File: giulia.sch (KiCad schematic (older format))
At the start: 129 parts, among them J1 AVR-ISP-6, J2 0548190519, SW1 RESET, SW2 BOOT, U1 ATmega32A-PU, Y1 16 MHz

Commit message: moved USB footprint to own lib
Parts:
- removed J2: 0548190519, digikey-footprints:USB_Mini_B_Female_548190519, symbol dk_USB-DVI-HDMI-Connectors:0548190519
- added J2: 0548190519, giulia:USB_Mini_B_Female_548190519, symbol giulia:0548190519
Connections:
- net GND: now also J2.1
- net VCC: now also J2.5
- net at D48.1 (K), R2.2: now also J2.3
- net at D49.1 (K), R3.2: now also J2.4
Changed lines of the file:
@@
 	5200 5850 5050 5850
-$Comp
-L dk_USB-DVI-HDMI-Connectors:0548190519 J2
-U 1 1 61732FEC
-P 4650 6950
-F 0 "J2" H 4675 7602 60  0000 C CNN
-F 1 "0548190519" H 4675 7496 60  0000 C CNN
-F 2 "digikey-footprints:USB_Mini_B_Female_548190519" H 4850 7150 60  0001 L CNN
-F 3 "https://www.molex.com/pdm_docs/sd/548190519_sd.pdf" H 4850 7250 60  0001 L CNN
-F 4 "WM17115-ND" H 4850 7350 60  0001 L CNN "Digi-Key_PN"
-F 5 "0548190519" H 4850 7450 60  0001 L CNN "MPN"
-F 6 "Connectors, Interconnects" H 4850 7550 60  0001 L CNN "Category"
-F 7 "USB, DVI, HDMI Connectors" H 4850 7650 60  0001 L CNN "Family"
-F 8 "https://www.molex.com/pdm_docs/sd/548190519_sd.pdf" H 4850 7750 60  0001 L CNN "DK_Datasheet_Link"
-F 9 "/product-detail/en/molex/0548190519/WM17115-ND/773802" H 4850 7850 60  0001 L CNN "DK_Detail_Page"
-F 10 "CONN RCPT USB2.0 MINI B 5P R/A" H 4850 7950 60  0001 L CNN "Description"
-F 11 "Molex" H 4850 8050 60  0001 L CNN "Manufacturer"
-F 12 "Active" H 4850 8150 60  0001 L CNN "Status"
-	1    4650 6950
-	1    0    0    -1
-$EndComp
 $Comp
 L power:VCC #PWR011
@@
 $EndComp
 Wire Wire Line
-	4950 7150 6300 7150
-Wire Wire Line
 	6300 7100 6300 7150
 Connection ~ 6300 7150
 Wire Wire Line
 	6300 7150 6450 7150
-Wire Wire Line
-	6750 6750 5850 6750
 Connection ~ 5850 7050
 Wire Wire Line
@@
 	1    0    0    -1
 $EndComp
+$Comp
+L giulia:0548190519 J2
+U 1 1 616D264C
+P 4650 6950
+F 0 "J2" H 4675 7602 60  0000 C CNN
+F 1 "0548190519" H 4675 7496 60  0000 C CNN
+F 2 "giulia:USB_Mini_B_Female_548190519" H 4850 7150 60  0001 L CNN
+F 3 "https://www.molex.com/pdm_docs/sd/548190519_sd.pdf" H 4850 7250 60  0001 L CNN
+F 4 "WM17115-ND" H 4850 7350 60  0001 L CNN "Digi-Key_PN"
+F 5 "0548190519" H 4850 7450 60  0001 L CNN "MPN"
+F 6 "Connectors, Interconnects" H 4850 7550 60  0001 L CNN "Category"
+F 7 "USB, DVI, HDMI Connectors" H 4850 7650 60  0001 L CNN "Family"
+F 8 "https://www.molex.com/pdm_docs/sd/548190519_sd.pdf" H 4850 7750 60  0001 L CNN "DK_Datasheet_Link"
+F 9 "/product-detail/en/molex/0548190519/WM17115-ND/773802" H 4850 7850 60  0001 L CNN "DK_Detail_Page"
+F 10 "CONN RCPT USB2.0 MINI B 5P R/A" H 4850 7950 60  0001 L CNN "Description"
+F 11 "Molex" H 4850 8050 60  0001 L CNN "Manufacturer"
+F 12 "Active" H 4850 8150 60  0001 L CNN "Status"
+	1    4650 6950
+	1    0    0    -1
+$EndComp
+Wire Wire Line
+	4950 7150 6300 7150
+Wire Wire Line
+	5850 6750 6750 6750
 $EndSCHEMATC

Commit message: some PCB finishing touches
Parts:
- D48, D49: footprint Diode_THT:D_DO-35_SOD27_P7.62mm_Horizontal -> giulia:D_DO-35_SOD27_P7.62mm_Zener
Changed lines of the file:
@@
 F 0 "D49" V 5950 6700 50  0000 L CNN
 F 1 "3,6 V" V 5850 6650 50  0000 L CNN
-F 2 "Diode_THT:D_DO-35_SOD27_P7.62mm_Horizontal" V 5850 6950 50  0001 C CNN
+F 2 "giulia:D_DO-35_SOD27_P7.62mm_Zener" V 5850 6950 50  0001 C CNN
 F 3 "~" V 5850 6950 50  0001 C CNN
 	1    5850 6950
@@
 F 0 "D48" V 5400 7050 50  0000 R CNN
 F 1 "3,6 V" V 5300 7100 50  0000 R CNN
-F 2 "Diode_THT:D_DO-35_SOD27_P7.62mm_Horizontal" V 5350 6850 50  0001 C CNN
+F 2 "giulia:D_DO-35_SOD27_P7.62mm_Zener" V 5350 6850 50  0001 C CNN
 F 3 "~" V 5350 6850 50  0001 C CNN
 	1    5350 6850

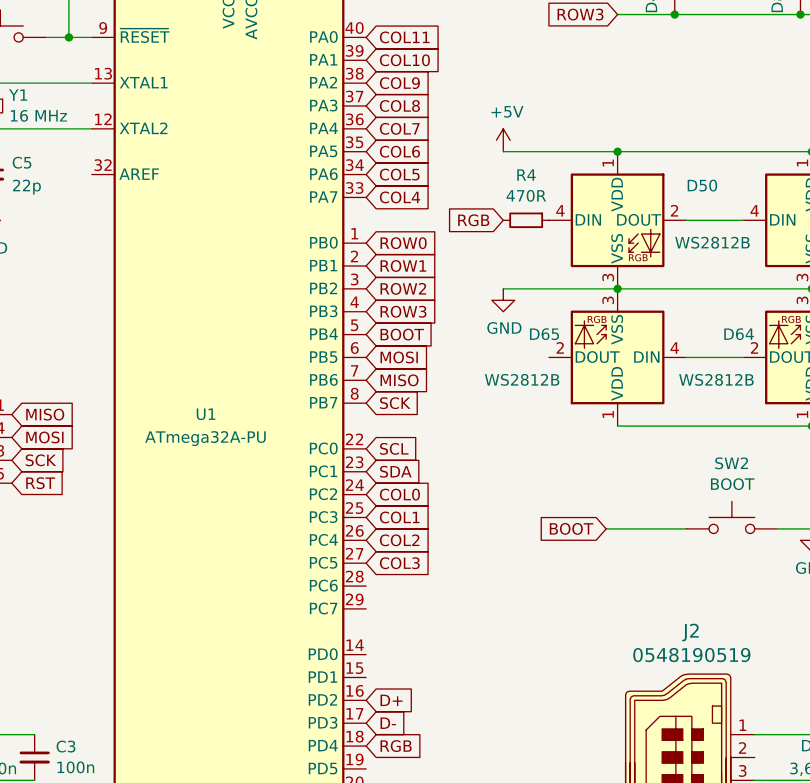
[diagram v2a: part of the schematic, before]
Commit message: moved cols 4,5 to better pins
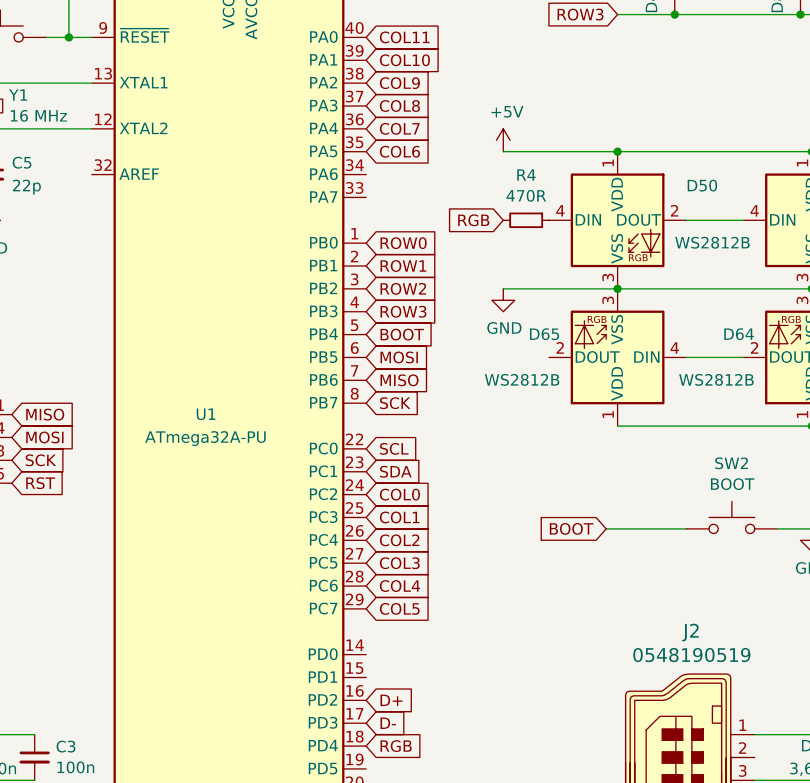
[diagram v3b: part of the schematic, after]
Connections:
- net COL4: now also U1.28 (PC6); no longer U1.33 (PA7)
- net COL5: now also U1.29 (PC7); no longer U1.34 (PA6)
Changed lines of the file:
@@
 Text GLabel 3250 6000 2    50   Input ~ 0
 COL3
-Text GLabel 3250 4400 2    50   Input ~ 0
+Text GLabel 3250 6100 2    50   Input ~ 0
 COL4
-Text GLabel 3250 4300 2    50   Input ~ 0
+Text GLabel 3250 6200 2    50   Input ~ 0
 COL5
 Text GLabel 3250 4200 2    50   Input ~ 0

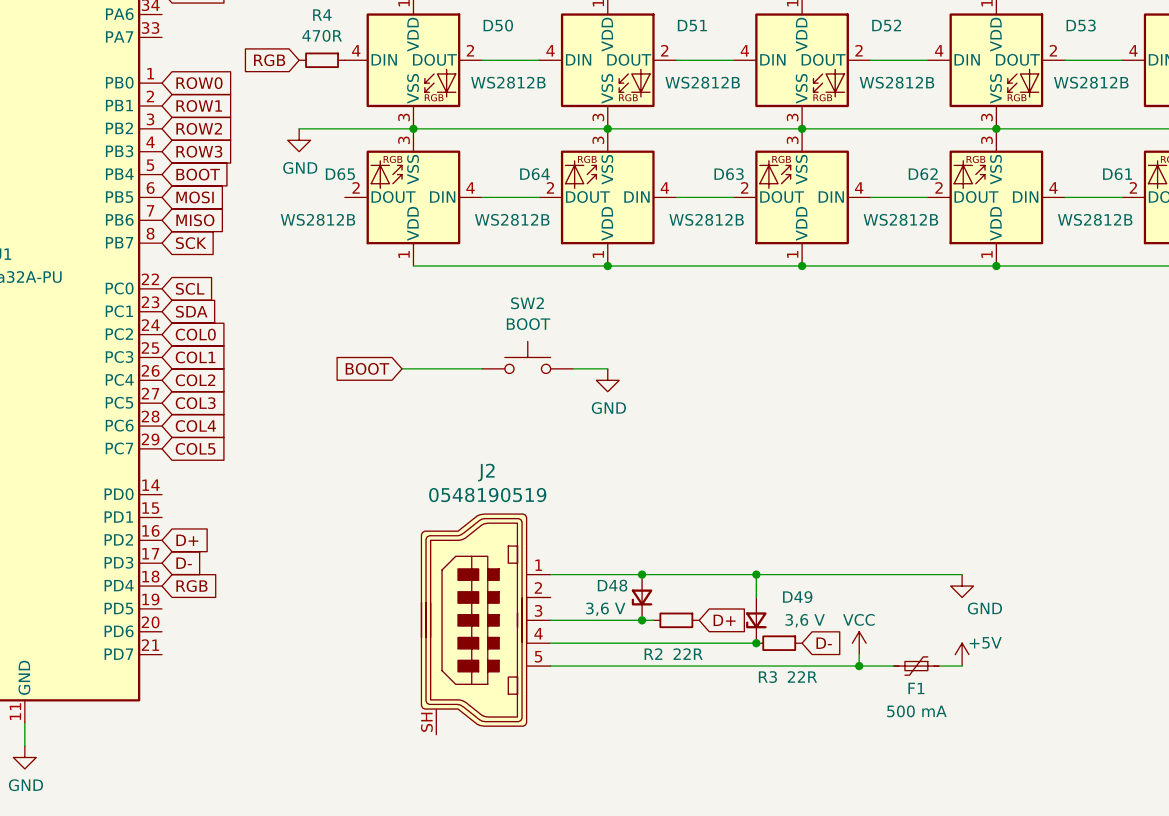
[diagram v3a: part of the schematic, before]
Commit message: fixed USB connector wiring
The original prototype is wired backwards...
Also moved boot button from B4 to D1, as having it on different port than USB seems to be giving the bootloader some trouble. This may get reversed if software fix is found.
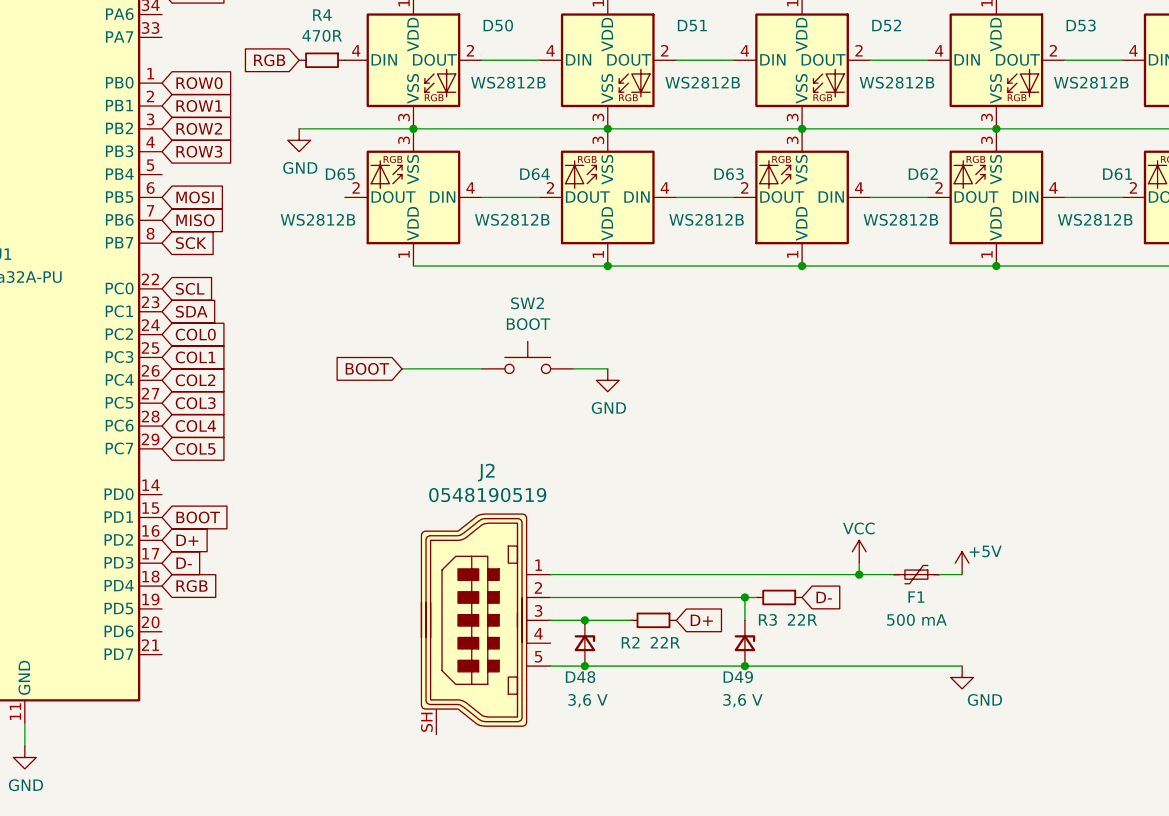
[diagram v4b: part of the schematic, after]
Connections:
- net BOOT: now also U1.15 (PD1); no longer U1.5 (PB4)
- net GND: now also J2.5; no longer J2.1
- net VCC: now also J2.1; no longer J2.5
- net at D49.1 (K), R3.2: now also J2.2; no longer J2.4
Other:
- moved on the sheet: D48, D49, F1, R2, R3
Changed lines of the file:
@@
 L Device:R_Small R2
 U 1 1 610FF916
-P 5500 6950
-F 0 "R2" V 5650 6850 50  0000 C CNN
-F 1 "22R" V 5650 7000 50  0000 C CNN
-F 2 "Resistor_THT:R_Axial_DIN0207_L6.3mm_D2.5mm_P10.16mm_Horizontal" H 5500 6950 50  0001 C CNN
-F 3 "~" H 5500 6950 50  0001 C CNN
-	1    5500 6950
+P 5400 6950
+F 0 "R2" V 5500 6850 50  0000 C CNN
+F 1 "22R" V 5500 7000 50  0000 C CNN
+F 2 "Resistor_THT:R_Axial_DIN0207_L6.3mm_D2.5mm_P10.16mm_Horizontal" H 5400 6950 50  0001 C CNN
+F 3 "~" H 5400 6950 50  0001 C CNN
+	1    5400 6950
 	0    1    1    0
 $EndComp
@@
 L Device:R_Small R3
 U 1 1 61100209
-P 5950 7050
-F 0 "R3" V 6100 7000 50  0000 C CNN
-F 1 "22R" V 6100 7150 50  0000 C CNN
-F 2 "Resistor_THT:R_Axial_DIN0207_L6.3mm_D2.5mm_P10.16mm_Horizontal" H 5950 7050 50  0001 C CNN
-F 3 "~" H 5950 7050 50  0001 C CNN
-	1    5950 7050
+P 5950 6850
+F 0 "R3" V 6050 6800 50  0000 C CNN
+F 1 "22R" V 6050 6950 50  0000 C CNN
+F 2 "Resistor_THT:R_Axial_DIN0207_L6.3mm_D2.5mm_P10.16mm_Horizontal" H 5950 6850 50  0001 C CNN
+F 3 "~" H 5950 6850 50  0001 C CNN
+	1    5950 6850
 	0    1    1    0
 $EndComp
@@
 L Device:Polyfuse_Small F1
 U 1 1 6113529C
-P 6550 7150
-F 0 "F1" V 6650 7150 50  0000 C CNN
-F 1 "500 mA" V 6750 7150 50  0000 C CNN
-F 2 "Fuse:Fuse_BelFuse_0ZRE0005FF_L8.3mm_W3.8mm" H 6600 6950 50  0001 L CNN
-F 3 "~" H 6550 7150 50  0001 C CNN
-	1    6550 7150
+P 6550 6750
+F 0 "F1" V 6650 6750 50  0000 C CNN
+F 1 "500 mA" V 6750 6750 50  0000 C CNN
+F 2 "Fuse:Fuse_BelFuse_0ZRE0005FF_L8.3mm_W3.8mm" H 6600 6550 50  0001 L CNN
+F 3 "~" H 6550 6750 50  0001 C CNN
+	1    6550 6750
 	0    1    1    0
 $EndComp
-Text GLabel 6050 7050 2    50   Input ~ 0
+Text GLabel 6050 6850 2    50   Input ~ 0
 D-
-Text GLabel 5600 6950 2    50   Input ~ 0
+Text GLabel 5500 6950 2    50   Input ~ 0
 D+
 $Comp
 L power:+5V #PWR013
 U 1 1 61136D2B
+P 6750 6750
+F 0 "#PWR013" H 6750 6600 50  0001 C CNN
+F 1 "+5V" H 6850 6850 50  0000 C CNN
+F 2 "" H 6750 6750 50  0001 C CNN
+F 3 "" H 6750 6750 50  0001 C CNN
+	1    6750 6750
+	1    0    0    -1
+$EndComp
+Wire Wire Line
+	6750 6750 6650 6750
+$Comp
+L power:GND #PWR012
+U 1 1 61138B5D
 P 6750 7150
-F 0 "#PWR013" H 6750 7000 50  0001 C CNN
-F 1 "+5V" H 6850 7250 50  0000 C CNN
+F 0 "#PWR012" H 6750 6900 50  0001 C CNN
+F 1 "GND" H 6850 7000 50  0000 C CNN
 F 2 "" H 6750 7150 50  0001 C CNN
 F 3 "" H 6750 7150 50  0001 C CNN
 	1    6750 7150
-	1    0    0    -1
-$EndComp
-Wire Wire Line
-	6750 7150 6650 7150
-$Comp
-L power:GND #PWR012
-U 1 1 61138B5D
-P 6750 6750
-F 0 "#PWR012" H 6750 6500 50  0001 C CNN
-F 1 "GND" H 6850 6600 50  0000 C CNN
-F 2 "" H 6750 6750 50  0001 C CNN
-F 3 "" H 6750 6750 50  0001 C CNN
-	1    6750 6750
 	1    0    0    -1
 $EndComp
@@
 L power:VCC #PWR011
 U 1 1 611378A5
-P 6300 7100
-F 0 "#PWR011" H 6300 6950 50  0001 C CNN
-F 1 "VCC" H 6300 7250 50  0000 C CNN
-F 2 "" H 6300 7100 50  0001 C CNN
-F 3 "" H 6300 7100 50  0001 C CNN
-	1    6300 7100
-	1    0    0    -1
-$EndComp
-Wire Wire Line
-	6300 7100 6300 7150
-Connection ~ 6300 7150
-Wire Wire Line
-	6300 7150 6450 7150
-Connection ~ 5850 7050
-Wire Wire Line
-	5850 7050 4950 7050
-Wire Wire Line
-	5850 6850 5850 6750
-Connection ~ 5850 6750
-Wire Wire Line
-	5400 6950 5350 6950
-Connection ~ 5350 6950
-Connection ~ 5350 6750
-Wire Wire Line
-	5350 6750 5850 6750
-$Comp
-L Device:D_Zener_Small D49
-U 1 1 611415AA
-P 5850 6950
-F 0 "D49" V 5950 6700 50  0000 L CNN
-F 1 "3,6 V" V 5850 6650 50  0000 L CNN
-F 2 "giulia:D_DO-35_SOD27_P7.62mm_Zener" V 5850 6950 50  0001 C CNN
-F 3 "~" V 5850 6950 50  0001 C CNN
-	1    5850 6950
-	0    -1   -1   0
-$EndComp
-Wire Wire Line
-	5350 6950 4950 6950
-$Comp
-L Device:D_Zener_Small D48
-U 1 1 6113EDE2
-P 5350 6850
-F 0 "D48" V 5400 7050 50  0000 R CNN
-F 1 "3,6 V" V 5300 7100 50  0000 R CNN
-F 2 "giulia:D_DO-35_SOD27_P7.62mm_Zener" V 5350 6850 50  0001 C CNN
-F 3 "~" V 5350 6850 50  0001 C CNN
-	1    5350 6850
-	0    -1   -1   0
-$EndComp
-Wire Wire Line
-	5350 6750 4950 6750
-Text GLabel 3250 5000 2    50   Input ~ 0
+P 6300 6700
+F 0 "#PWR011" H 6300 6550 50  0001 C CNN
+F 1 "VCC" H 6300 6850 50  0000 C CNN
+F 2 "" H 6300 6700 50  0001 C CNN
+F 3 "" H 6300 6700 50  0001 C CNN
+	1    6300 6700
+	1    0    0    -1
+$EndComp
+Wire Wire Line
+	6300 6700 6300 6750
+Connection ~ 6300 6750
+Wire Wire Line
+	6300 6750 6450 6750
+Wire Wire Line
+	5850 6850 5800 6850
+Text GLabel 3250 6500 2    50   Input ~ 0
 BOOT
 Text GLabel 4300 5850 0    50   Input ~ 0
@@
 $EndComp
 Wire Wire Line
-	4950 7150 6300 7150
-Wire Wire Line
-	5850 6750 6750 6750
+	4950 7150 5100 7150
+$Comp
+L Device:D_Zener_Small D49
+U 1 1 611415AA
+P 5800 7050
+F 0 "D49" V 5950 6950 50  0000 L CNN
+F 1 "3,6 V" V 6050 6950 50  0000 L CNN
+F 2 "giulia:D_DO-35_SOD27_P7.62mm_Zener" V 5800 7050 50  0001 C CNN
+F 3 "~" V 5800 7050 50  0001 C CNN
+	1    5800 7050
+	0    1    1    0
+$EndComp
+$Comp
+L Device:D_Zener_Small D48
+U 1 1 6113EDE2
+P 5100 7050
+F 0 "D48" V 5250 7100 50  0000 R CNN
+F 1 "3,6 V" V 5350 7150 50  0000 R CNN
+F 2 "giulia:D_DO-35_SOD27_P7.62mm_Zener" V 5100 7050 50  0001 C CNN
+F 3 "~" V 5100 7050 50  0001 C CNN
+	1    5100 7050
+	0    1    1    0
+$EndComp
+Wire Wire Line
+	4950 6950 5100 6950
+Connection ~ 5100 6950
+Wire Wire Line
+	5100 6950 5300 6950
+Connection ~ 5100 7150
+Wire Wire Line
+	5100 7150 5800 7150
+Connection ~ 5800 7150
+Wire Wire Line
+	5800 7150 6750 7150
+Wire Wire Line
+	5800 6950 5800 6850
+Wire Wire Line
+	4950 6750 6300 6750
+Connection ~ 5800 6850
+Wire Wire Line
+	5800 6850 4950 6850
 $EndSCHEMATC
